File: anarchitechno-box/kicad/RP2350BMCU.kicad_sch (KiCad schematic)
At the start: 51 parts, among them J1 GT-USB-7010ASV, J10 Conn_01x04, J2 Conn_01x03_Socket, J8 Conn_01x04, Q1 12MHz, SW1 C318884, SW2 RotaryEncoder_Switch_MP, U4 RMC20452T, U6 TLV74311PDBVR, U7 SRV05-4-P-T7

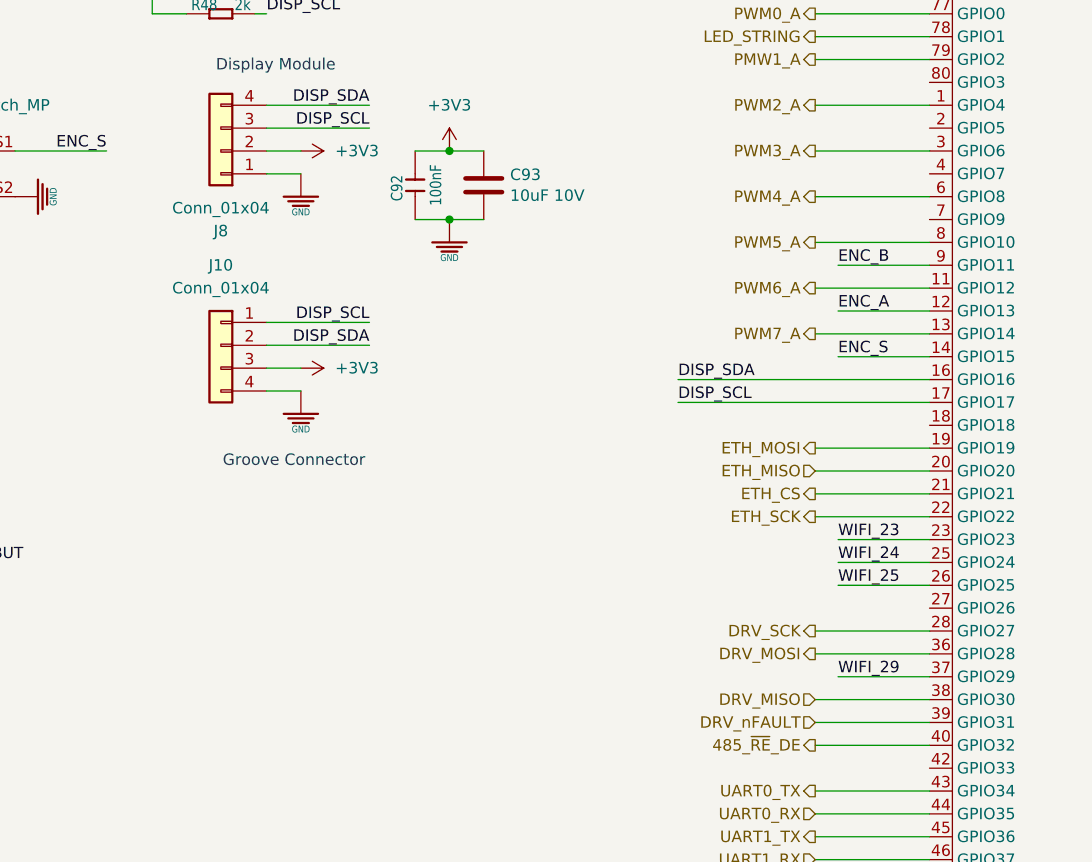
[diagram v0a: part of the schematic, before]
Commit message: - Logo Robot Theater lab - UART connector - RF antenne clearance aangepast - Reset/interrupt pins ethernet aangesloten
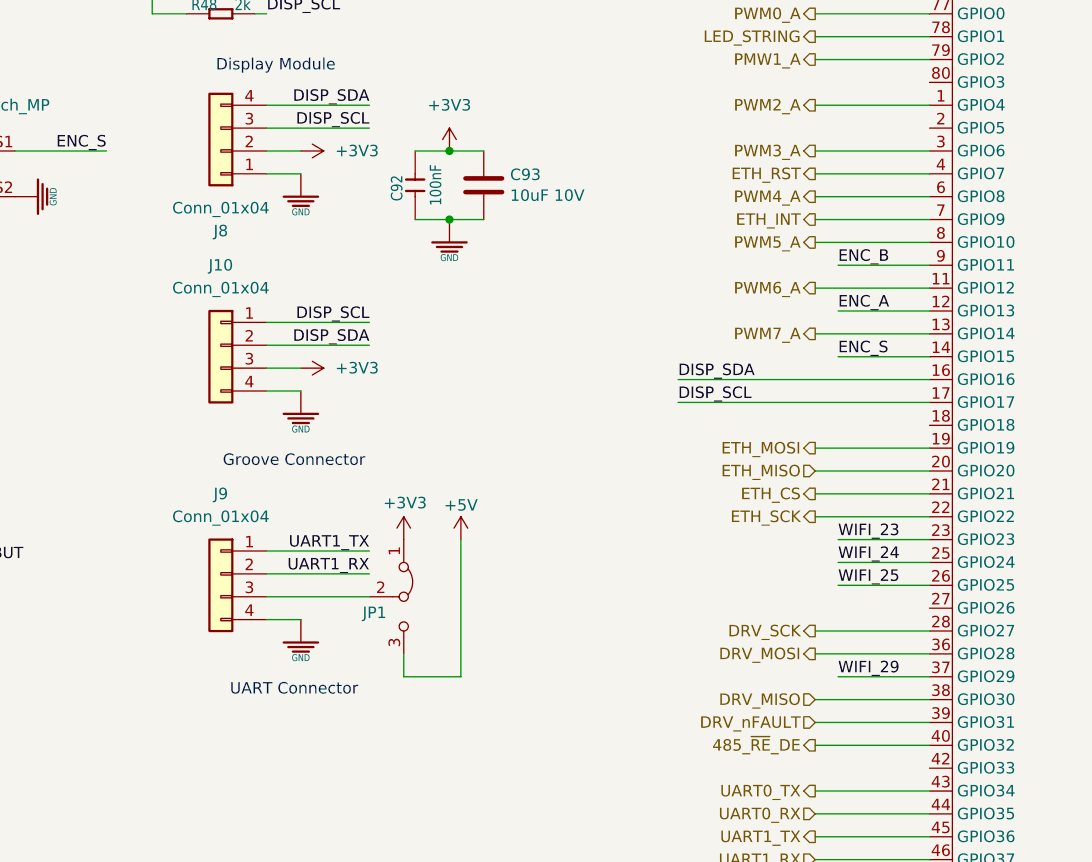
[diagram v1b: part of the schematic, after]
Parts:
- added J9: Conn_01x04, Connectors:Grove_1x04, symbol Connector_Generic:Conn_01x04
- added JP1: Jumper_3_Bridged12, Jumper:SolderJumper-3_P1.3mm_Bridged12_RoundedPad1.0x1.5mm, symbol Jumper:Jumper_3_Bridged12
- J8: footprint Connector_PinHeader_2.54mm:PinHeader_1x04_P2.54mm_Vertical -> Connector_PinSocket_2.54mm:PinSocket_1x04_P2.54mm_Vertical
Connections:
- net +3V3: now also JP1.1 (A)
- net +5V: now also JP1.3 (B)
- net GND: now also J9.4 (Pin_4)
- net UART1_RX: now also J9.2 (Pin_2)
- net UART1_TX: now also J9.1 (Pin_1)
- net ETH_RST: now reaches U8.4 (GPIO7)
- net ETH_INT: now reaches U8.7 (GPIO9)
- new net: J9.3 (Pin_3), JP1.2 (C)
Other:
- note added: "UART Connector"

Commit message: BOM nagelopen, bestelklaar.
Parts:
- C19: LCSC Part (none) -> C52923; LSCS Part C52923 -> (none)
- D16: LCSC Part (none) -> C8678
- J10, J9: now not fitted; now left out of the parts list
- J2: LCSC Part (none) -> C160403
- J8: LCSC Part (none) -> C7509546
- R4, R5: footprint Resistor_SMD:R_0402_1005Metric -> Resistor_SMD:R_0603_1608Metric
- R47, R48: value 2k -> 1k
- R6: now left out of the parts list
- U8: value ~ -> RP2350B
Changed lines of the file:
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@@
 		(unit 1)
 		(exclude_from_sim no)
-		(in_bom yes)
+		(in_bom no)
 		(on_board yes)
 		(dnp yes)
@@
 			)
 		)
+		(property "LCSC Part" "C7509546"
+			(at 300.99 107.95 0)
+			(effects
+				(font
+					(size 1.27 1.27)
+				)
+				(hide yes)
+			)
+		)
 		(pin "2"
 		)
@@
 			)
 		)
-		(property "Value" "2k"
+		(property "Value" "1k"
 			(at 302.514 89.916 0)
 			(effects
@@
 			)
 		)
+		(property "LCSC Part" "C160403"
+			(at 311.15 33.02 0)
+			(effects
+				(font
+					(size 1.27 1.27)
+				)
+				(hide yes)
+			)
+		)
 		(pin "1"
 		)
@@
 			)
 		)
-		(property "Footprint" "Resistor_SMD:R_0402_1005Metric"
+		(property "Footprint" "Resistor_SMD:R_0603_1608Metric"
 			(at 193.04 266.7 0)
 			(effects
@@
 		(unit 1)
 		(exclude_from_sim no)
-		(in_bom yes)
+		(in_bom no)
 		(on_board yes)
-		(dnp no)
+		(dnp yes)
 		(property "Reference" "J10"
 			(at 300.99 120.65 0)
@@
 			)
 		)
-		(property "Footprint" "Resistor_SMD:R_0402_1005Metric"
+		(property "Footprint" "Resistor_SMD:R_0603_1608Metric"
 			(at 200.66 266.7 0)
 			(effects
@@
 			)
 		)
+		(property "LCSC Part" "C8678"
+			(at 205.74 214.63 0)
+			(effects
+				(font
+					(size 1.27 1.27)
+				)
+				(hide yes)
+			)
+		)
 		(pin "2"
 		)
@@
 			)
 		)
-		(property "Value" "~"
+		(property "Value" "RP2350B"
 			(at 400.05 133.35 0)
 			(effects
@@
 		(unit 1)
 		(exclude_from_sim no)
-		(in_bom yes)
+		(in_bom no)
 		(on_board yes)
-		(dnp no)
+		(dnp yes)
 		(property "Reference" "J9"
 			(at 300.99 146.05 0)
@@
 			)
 		)
-		(property "Value" "2k"
+		(property "Value" "1k"
 			(at 302.514 92.456 0)
 			(effects
@@
 			)
 		)
-		(property "LSCS Part" "C52923"
+		(property "LCSC Part" "C52923"
 			(at 114.3 34.29 0)
 			(effects
